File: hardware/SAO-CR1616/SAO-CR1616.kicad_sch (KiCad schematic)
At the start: 34 parts, among them J1 Conn_01x03, J2 SAO v1.69bis addon, U1 WCH CH32V003F4U6

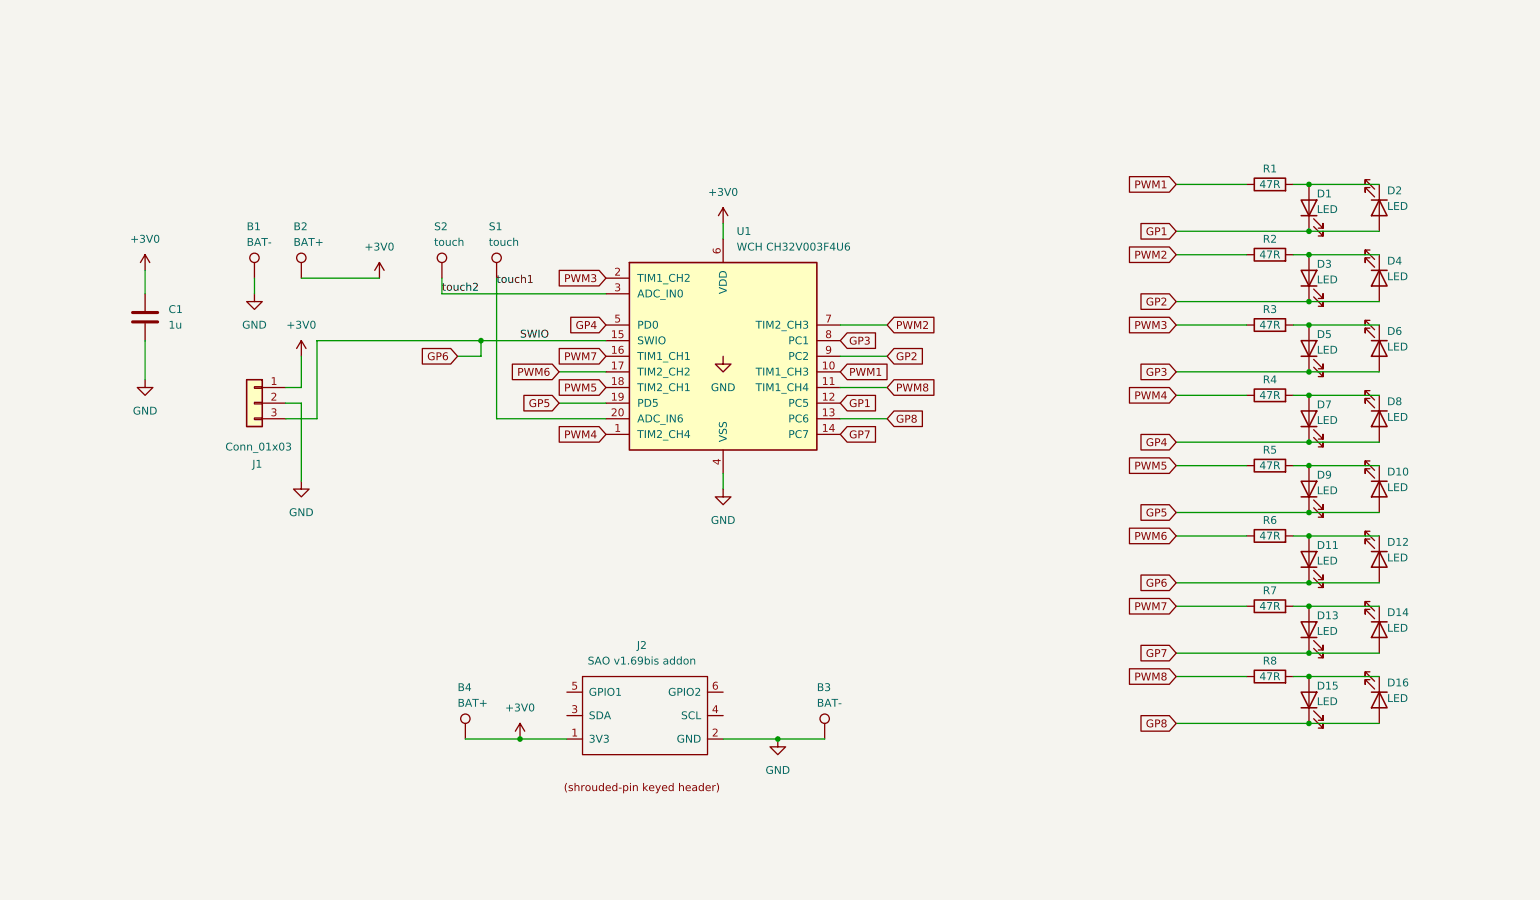
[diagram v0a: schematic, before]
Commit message: separate into fab-able parts
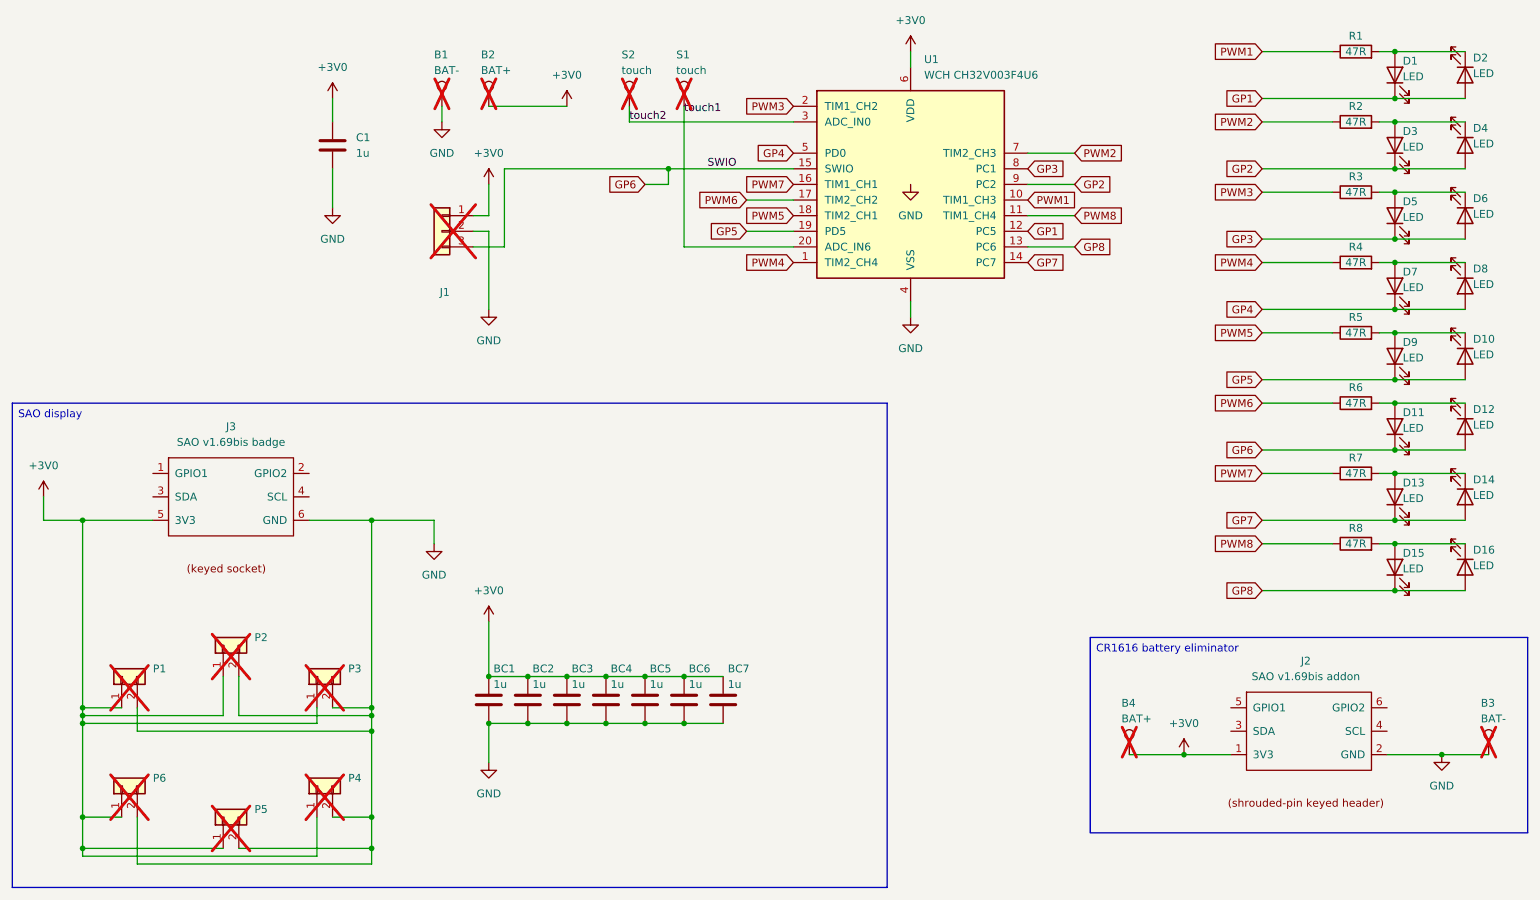
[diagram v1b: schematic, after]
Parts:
- added BC1, BC2, BC3, BC4, BC5, BC6, BC7: 1u, Capacitor_SMD:C_0805_2012Metric_Pad1.18x1.45mm_HandSolder, symbol Device:C
- added J3: SAO v1.69bis badge, Connector_IDC:IDC-Header_2x03_P2.54mm_Vertical, symbol extra:SAO v1.69bis badge
- added P1, P2, P3, P4, P5, P6: Conn_01x02, Connector_PinHeader_2.54mm:PinHeader_1x02_P2.54mm_Vertical, symbol Connector_Generic:Conn_01x02
- B1, B2, B3, B4, J1, S1, S2: now not fitted
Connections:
- net +3V0: now also BC1.1, BC2.1, BC3.1, BC4.1, BC5.1, BC6.1, BC7.1, J3.5 (3V3), P1.1 (Pin_1), P2.1 (Pin_1), P3.1 (Pin_1), P4.1 (Pin_1), P5.1 (Pin_1), P6.1 (Pin_1)
- net GND: now also BC1.2, BC2.2, BC3.2, BC4.2, BC5.2, BC6.2, BC7.2, J3.6 (GND), P1.2 (Pin_2), P2.2 (Pin_2), P3.2 (Pin_2), P4.2 (Pin_2), P5.2 (Pin_2), P6.2 (Pin_2)
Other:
- moved on the sheet: C1, D1, D10, D11, D12, D13, D14, D15, D16, D2, D3, D4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
